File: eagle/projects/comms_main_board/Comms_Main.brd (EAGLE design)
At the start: 101.6 x 95.2 mm, 201 parts, among them J1 WRL-00593, J10 MOL-SL-2-RA, J11 MOL-SL-3-RA, J12 MOL-SL-3-RA, J13 MOL-SL-3-RA, J14 MOL-SL-3-RA, J15 MOL-SL-2-RA, J16 MOL-MINIJR-2P-RA, J17 MOL-MINIJR-2P-RA, J18 MOL-MINIJR-2P-RA, J19 MOL-MINIJR-2P-RA, J2 PRT-12639, J20 MOL-SL-2-RA, J21 RECEPTACLE-2x2-254MM, J22 MOL-SL-2-RA, J3 PRT-12639, J4 PRT-12639, J5 PRT-12639, J6 MOL-SL-3-RA, J7 MOL-SL-5-RA, J8 RECEPTACLE-2x20-254MM, J9 MOL-SL-3-RA, Q1 CSD17579Q3A, U1 TPS562209DDCT, U10 MCP4541-103E/MS, U11 TPS562209DDCT, U12 MMBT3904-HF, U13 MAX3232CSE+, U14 MAX4311, U15 MAX6371, U16 2N7002P,215, U2 LP2985-33DBVR, U3 LP5900TLX-3.3/NOPB, U4 TPS562209DDCT, U5 NDT2955, U6 LM3488MMX/NOPB, U7 PCT2075D,118, U8 MS560702BA03-50, U9 MAX-M8Q

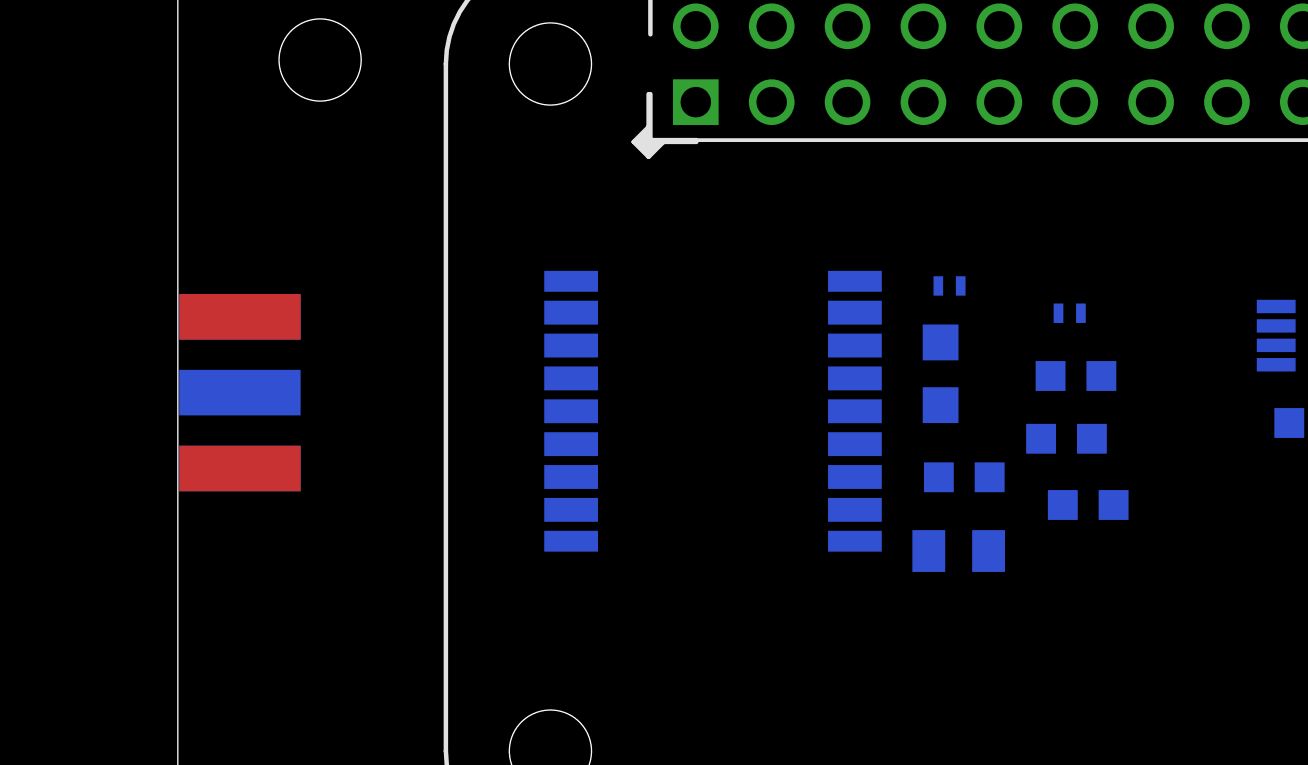
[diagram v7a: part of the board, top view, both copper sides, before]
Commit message: routing gps module
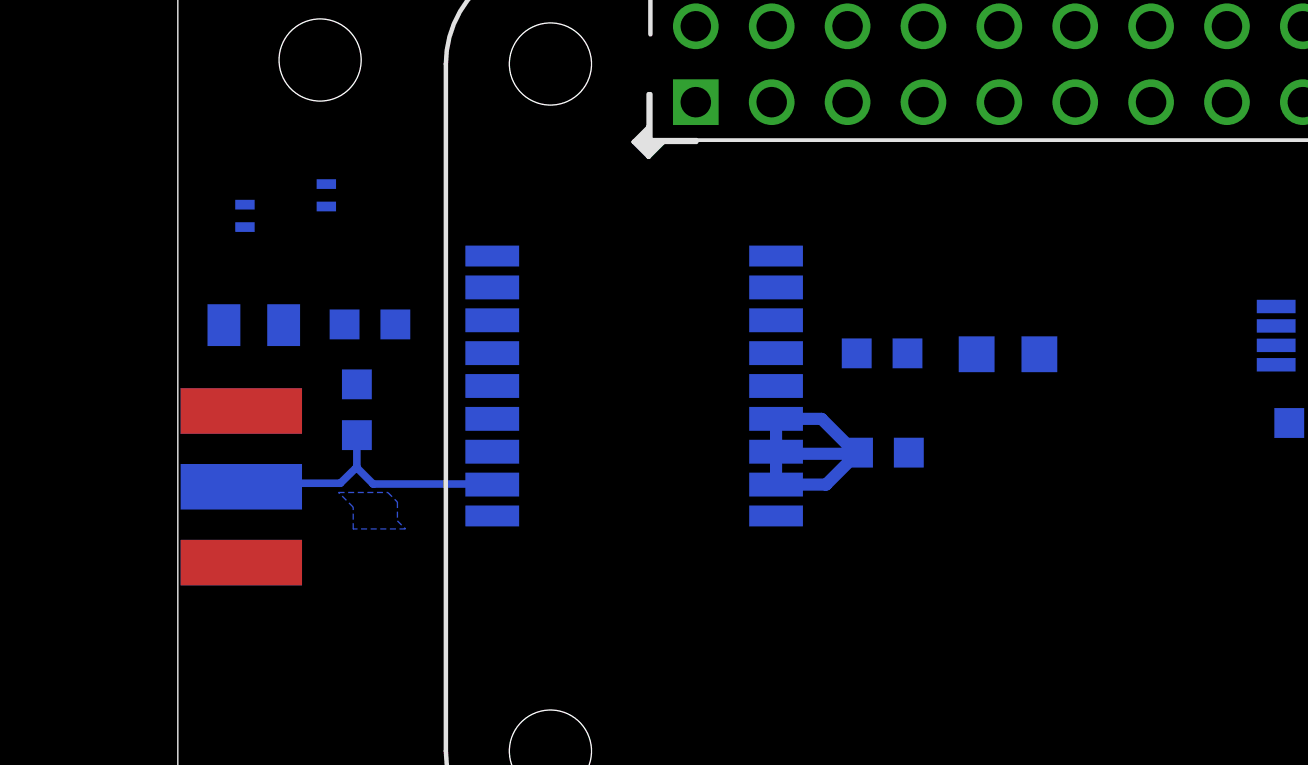
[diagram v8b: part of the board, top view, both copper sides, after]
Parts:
- moved FB1 27.8 mm to (2.25, 85.3), turned to 270 degrees
- moved C22 24.8 mm to (2.54, 81.6)
- moved L5 24.7 mm to (5.99, 78.8), turned to 90 degrees
- moved R16 23.6 mm to (6.43, 81.6), turned to 180 degrees
- moved FB2 21.1 mm to (4.97, 86.0), turned to 270 degrees
- moved R17 6.53 mm to (23.6, 80.7), turned to 180 degrees
- moved J1 3.15 mm to (2.12, 73.7)
- moved U9 3.13 mm to (15.1, 79.5), turned to 180 degrees
- moved C27 2.83 mm to (23.6, 77.3), turned to 180 degrees
- moved LED1 2.35 mm to (27.8, 80.6), turned to 90 degrees
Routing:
- net 3P3V_SENSORS: track 0.00 -> 11.3 mm
- net GPS_ANTENNA: track 0.00 -> 10.1 mm
- added copper zone on layer 16, net N$1
